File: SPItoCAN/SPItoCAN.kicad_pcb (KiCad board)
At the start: 2 copper layers, 16 parts, among them J1 CONN_01x02, J2 CONN_01x02, J3 Conn1, J4 Conn, U1 TJA1051T-E, U2 MCP2515, Y1 8MHz

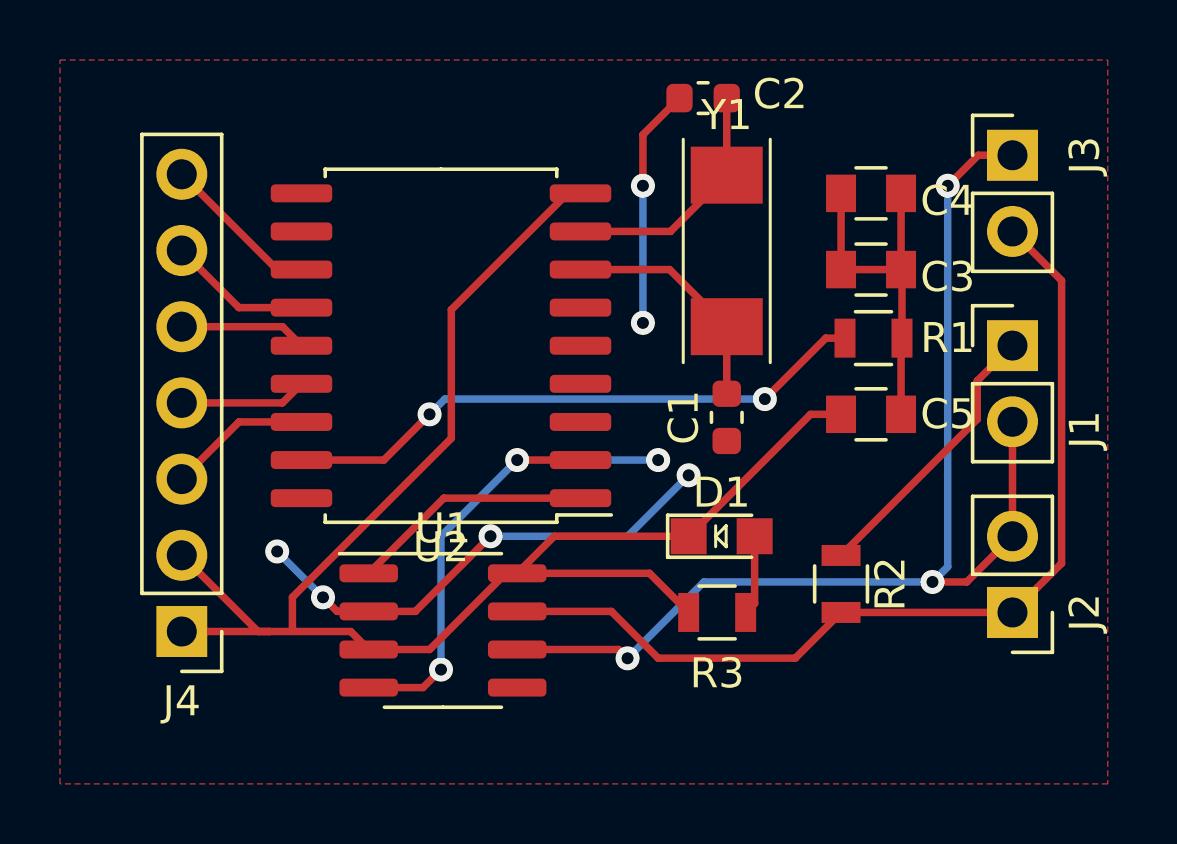
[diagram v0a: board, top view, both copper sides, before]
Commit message: Cleaned up PCB layout, added ground plane
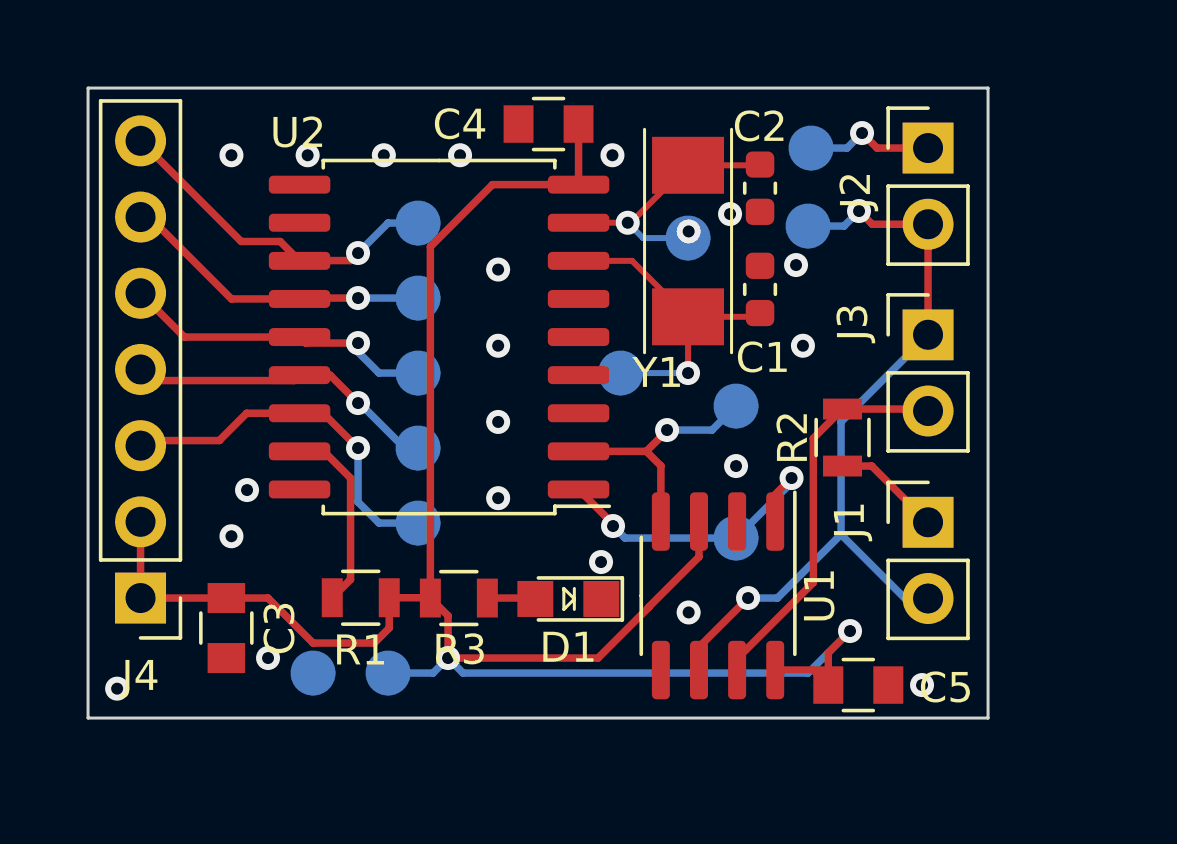
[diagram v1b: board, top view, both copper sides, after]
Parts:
- added CANH: Test_Point_SMD, TestPoint:TestPoint_Pad_D1.5mm, B.Cu at (37.1, 15.0)
- added CANL: Test_Point_SMD, TestPoint:TestPoint_Pad_D1.5mm, B.Cu at (37.0, 17.6)
- added CS: Test_Point_SMD, TestPoint:TestPoint_Pad_D1.5mm, B.Cu at (24.0, 27.5)
- added GND: Test_Point_SMD, TestPoint:TestPoint_Pad_D1.5mm, B.Cu at (20.5, 32.5)
- added INT: Test_Point_SMD, TestPoint:TestPoint_Pad_D1.5mm, B.Cu at (24.0, 17.5)
- added OSC+: Test_Point_SMD, TestPoint:TestPoint_Pad_D1.5mm, B.Cu at (33.0, 18.0)
- added OSC-: Test_Point_SMD, TestPoint:TestPoint_Pad_D1.5mm, B.Cu at (30.8, 22.5)
- added RXCAN: Test_Point_SMD, TestPoint:TestPoint_Pad_D1.5mm, B.Cu at (34.6, 23.6)
- added SCK: Test_Point_SMD, TestPoint:TestPoint_Pad_D1.5mm, B.Cu at (24.0, 20.0)
- added SI: Test_Point_SMD, TestPoint:TestPoint_Pad_D1.5mm, B.Cu at (24.0, 22.5)
- added SO: Test_Point_SMD, TestPoint:TestPoint_Pad_D1.5mm, B.Cu at (24.0, 25.0)
- added TXCAN: Test_Point_SMD, TestPoint:TestPoint_Pad_D1.5mm, B.Cu at (34.6, 28.0)
- added VCC: Test_Point_SMD, TestPoint:TestPoint_Pad_D1.5mm, B.Cu at (23.0, 32.5)
- C1, C2: value 22pF -> C_22pF
- J3: value Conn1 -> CONN_01x02
- J4: value Conn -> Conn_01x07
- U2: value MCP2515 -> MCP2515-xSO
- Y1: value 8MHz -> Crystal_8MHz
- moved C3 24.6 mm to (17.6, 31.0), turned to -90 degrees
- moved R1 19.2 mm to (22.1, 30.0)
- moved J2 15.7 mm to (41.0, 15.0), turned to 0 degrees
- moved C4 11.0 mm to (28.4, 14.2), turned to 180 degrees
- moved U1 9.24 mm to (34.0, 29.9), turned to -90 degrees
- moved C5 9.03 mm to (38.7, 32.9)
- moved R3 8.62 mm to (25.4, 30.0)
- moved J3 6.61 mm to (41.0, 21.2)
- moved J1 6.53 mm to (41.0, 27.5)
- moved D1 5.52 mm to (29.0, 30.0), turned to 180 degrees
- moved R2 4.88 mm to (38.1, 24.6), turned to 90 degrees
- moved C1 4.41 mm to (35.4, 19.7), turned to -90 degrees
- moved C2 3.55 mm to (35.4, 16.3), turned to 90 degrees
- moved J4 1.77 mm to (14.8, 30.0)
- moved Y1 1.33 mm to (33.0, 15.6)
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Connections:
- net /OSC1 renamed /OSC+
- net /OSC2 renamed /OSC-
- C3 pad 2: VCC -> GND
- C4 pad 2: VCC -> GND
- C5 pad 2: VCC -> GND
- D1 pad 1: VCC -> GND
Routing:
- net GND: track 27.0 -> 0.00 mm, vias 7 -> 20
- net /CANH: track 31.8 -> 17.7 mm, vias 0 -> 1
- net Net-(R1-Pad1): track 19.8 -> 6.31 mm, vias 2 -> 0
- net /CANL: track 38.1 -> 26.8 mm, vias 3 -> 2
- net /CS: track 4.78 -> 12.3 mm, vias 0 -> 1
- net /SI: track 4.25 -> 10.5 mm, vias 0 -> 1
- net /SO: track 4.25 -> 10.5 mm, vias 0 -> 1
- net /INT: track 5.31 -> 11.4 mm, vias 0 -> 1
- net Net-(J1-Pad1): track 9.36 -> 3.63 mm
- net /SCK: track 4.78 -> 10.4 mm, vias 0 -> 1
- net /RXCAN: track 12.8 -> 8.58 mm, vias 2 -> 1
- net /OSC-: track 7.90 -> 11.1 mm, vias 0 -> 1
- net /TXCAN: track 8.10 -> 10.5 mm, vias 0 -> 2
- net VCC: track 66.7 -> 67.8 mm, vias 0 -> 2
- net Net-(D1-Pad2): track 2.66 -> 1.61 mm
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- added copper zone on B.Cu, net GND
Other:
- board outline added: 30 x 21 mm

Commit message: cleaned up pcb, improved silkscreen, ran test gerber export
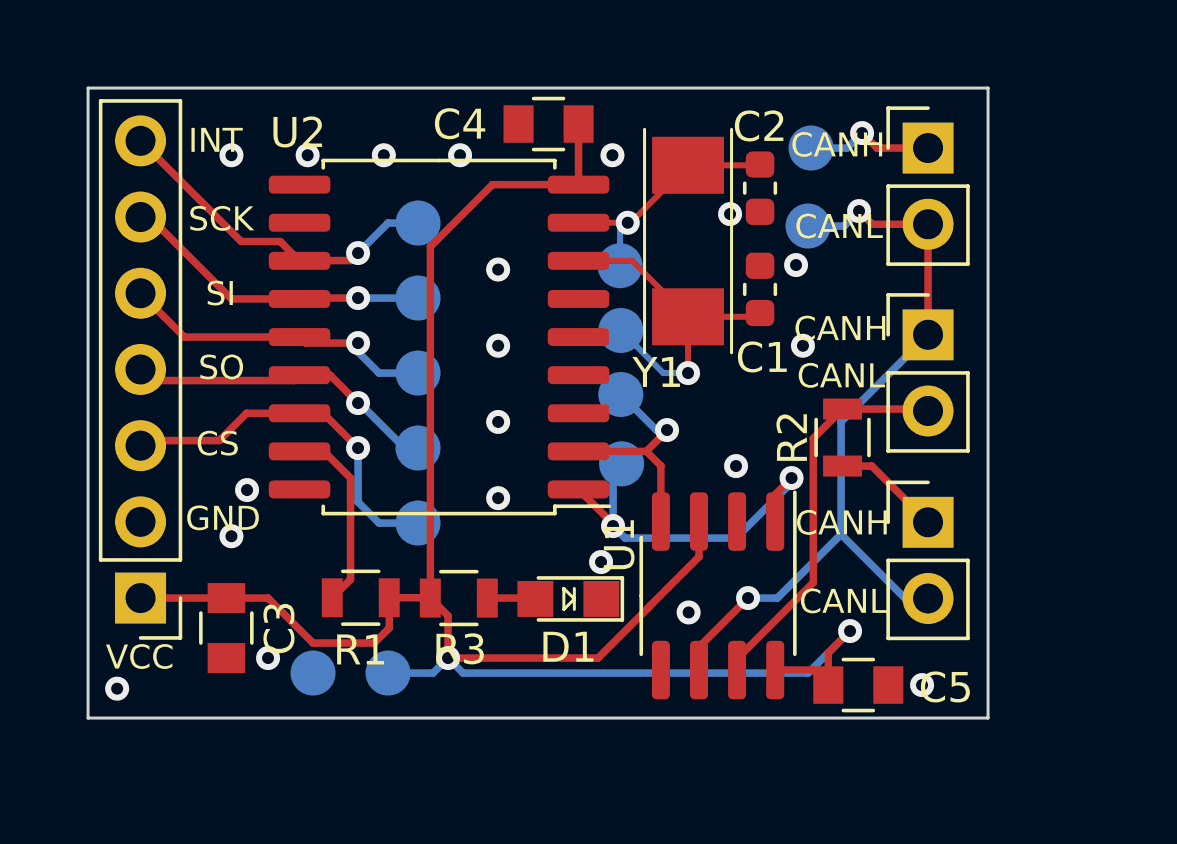
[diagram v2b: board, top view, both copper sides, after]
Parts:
- added G***: LOGO, Baja:12mm_baja_logo, B.Cu at (33.3, 30.8)
- moved TXCAN 4.55 mm to (30.8, 25.5)
- moved RXCAN 3.86 mm to (30.8, 23.2)
- moved OSC+ 2.45 mm to (30.7, 18.9)
- moved OSC- 1.42 mm to (30.8, 21.1)
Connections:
- J4 pad 2: VCC -> GND
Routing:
- net VCC: track 67.8 -> 65.3 mm
- net /TXCAN: track 10.5 -> 12.7 mm
- net /OSC+: track 9.11 -> 8.43 mm, vias 2 -> 1
- net /RXCAN: track 8.58 -> 7.98 mm
- net /OSC-: track 11.1 -> 11.7 mm
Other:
- board text added: "CANH"
- board text added: "CANL"
- board text added: "CS"
- board text added: "GND"
- board text added: "INT"
- board text added: "SCK"
- board text added: "SI"
- board text added: "SO"
- board text added: "SPI to CAN Converter v1 Designed by Carter Harris 2022"
- board text added: "VCC"

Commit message: cleaned up layout; replaced LED; generated BOM
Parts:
- removed the G*** at (33.3, 30.8)
- added G***: LOGO, Baja:16mm_phoenix, B.Cu at (33.4, 27.7)
- D1: value LED_0805_Red -> e; footprint footprints:LED_0805_OEM -> Baja:LED_0805_Red
- renumbered GND to GND1, VCC to VCC1
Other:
- board text removed: "SPI to CAN Converter v1 Designed by Carter Harris 2022"

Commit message: Fixed some wiring & routing across the board; added explanatory notes to schematic
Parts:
- D1: value e -> LED_0805_Red
- U1: footprint Package_SO:SOIC-8_3.9x4.9mm_P1.27mm -> Baja:SOIC127P600X175-8N
- moved C4 19.4 mm to (21.9, 32.5)
- moved C5 10.3 mm to (28.4, 32.5)
- renumbered GND1 to GND, VCC1 to VCC
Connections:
- U1 pad 8: VCC -> GND
- U2 pad 18: GND -> VCC
- U2 pad 9: VCC -> GND
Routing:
- net VCC: track 65.3 -> 36.8 mm, vias 2 -> 3
- net /TXCAN: track 12.7 -> 11.6 mm
- net GND: track 0.00 -> 0.30 mm, vias 20 -> 19

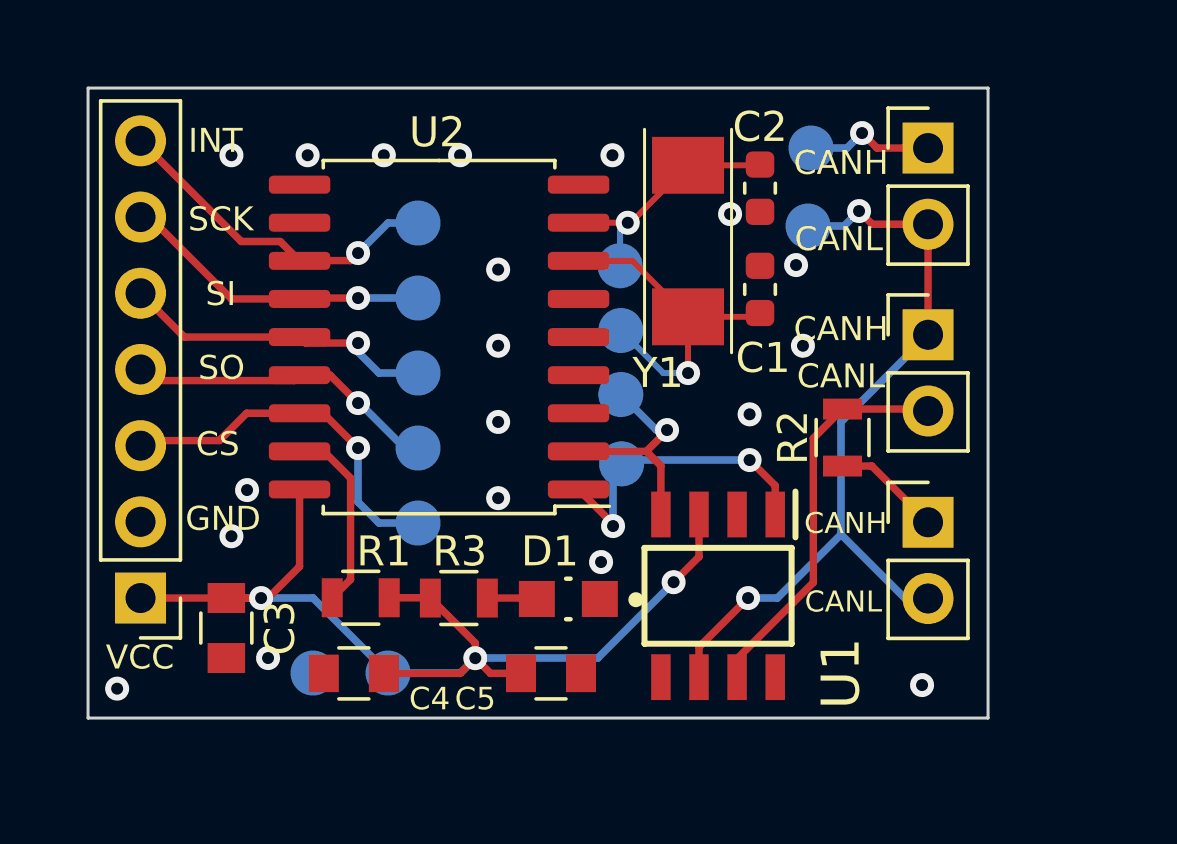
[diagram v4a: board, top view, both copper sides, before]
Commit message: Began tweaks to make everything fit within JLCPCB capabilites
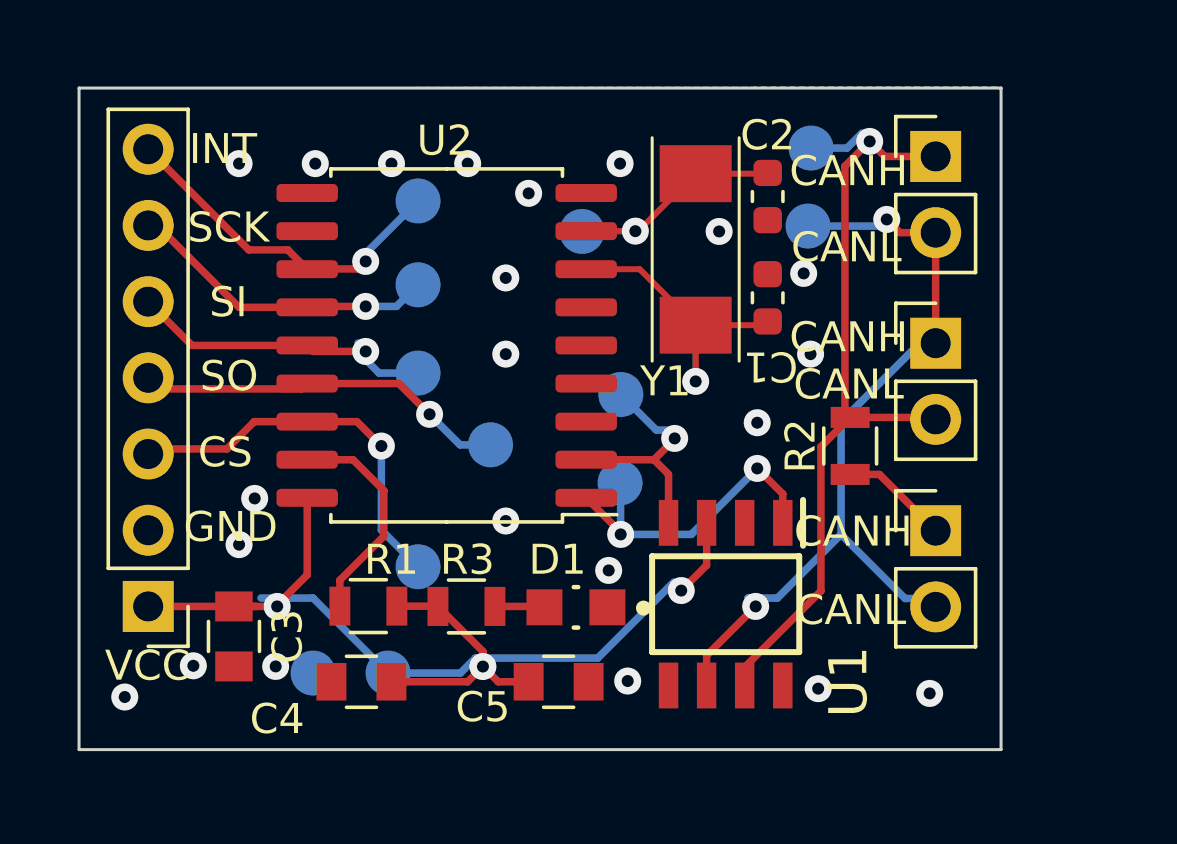
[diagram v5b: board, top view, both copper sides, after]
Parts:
- moved OSC- 2.53 mm to (33.3, 20.8)
- moved SO 2.42 mm to (26.4, 24.9)
- moved OSC+ 1.71 mm to (29.5, 17.8)
- moved CS 1.46 mm to (24.0, 29.0)
- moved INT 0.74 mm to (24.0, 16.8)
- moved TXCAN 0.64 mm to (30.7, 26.2)
- moved G*** 0.53 mm to (33.4, 28.2)
- moved SCK 0.44 mm to (24.0, 19.6)
- moved C1 0.38 mm to (35.7, 20.0)
- moved C2 0.38 mm to (35.7, 16.6)
- moved R2 0.38 mm to (38.4, 24.9)
- moved C4 0.38 mm to (22.1, 32.8)
- moved C5 0.38 mm to (28.7, 32.8)
- moved R1 0.38 mm to (22.3, 30.3)
- moved C3 0.38 mm to (17.9, 31.3)
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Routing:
- net /CANH: track 17.7 -> 27.3 mm
- net /SO: track 10.5 -> 12.5 mm
- net Net-(R1-Pad1): track 6.31 -> 7.44 mm
- net /OSC-: track 11.7 -> 10.8 mm
- net /CS: track 12.3 -> 13.1 mm
- net /TXCAN: track 11.6 -> 12.3 mm
- net GND: vias 19 -> 22
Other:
- board size 30 x 21 mm -> 30.7 x 22.1 mm
- board text added: "Olin Baja - 22-23"
- board text added: "SPI to CAN Adapter"
